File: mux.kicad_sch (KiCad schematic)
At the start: 22 parts, among them U24002 4066, U24003 4066, U24004 4075

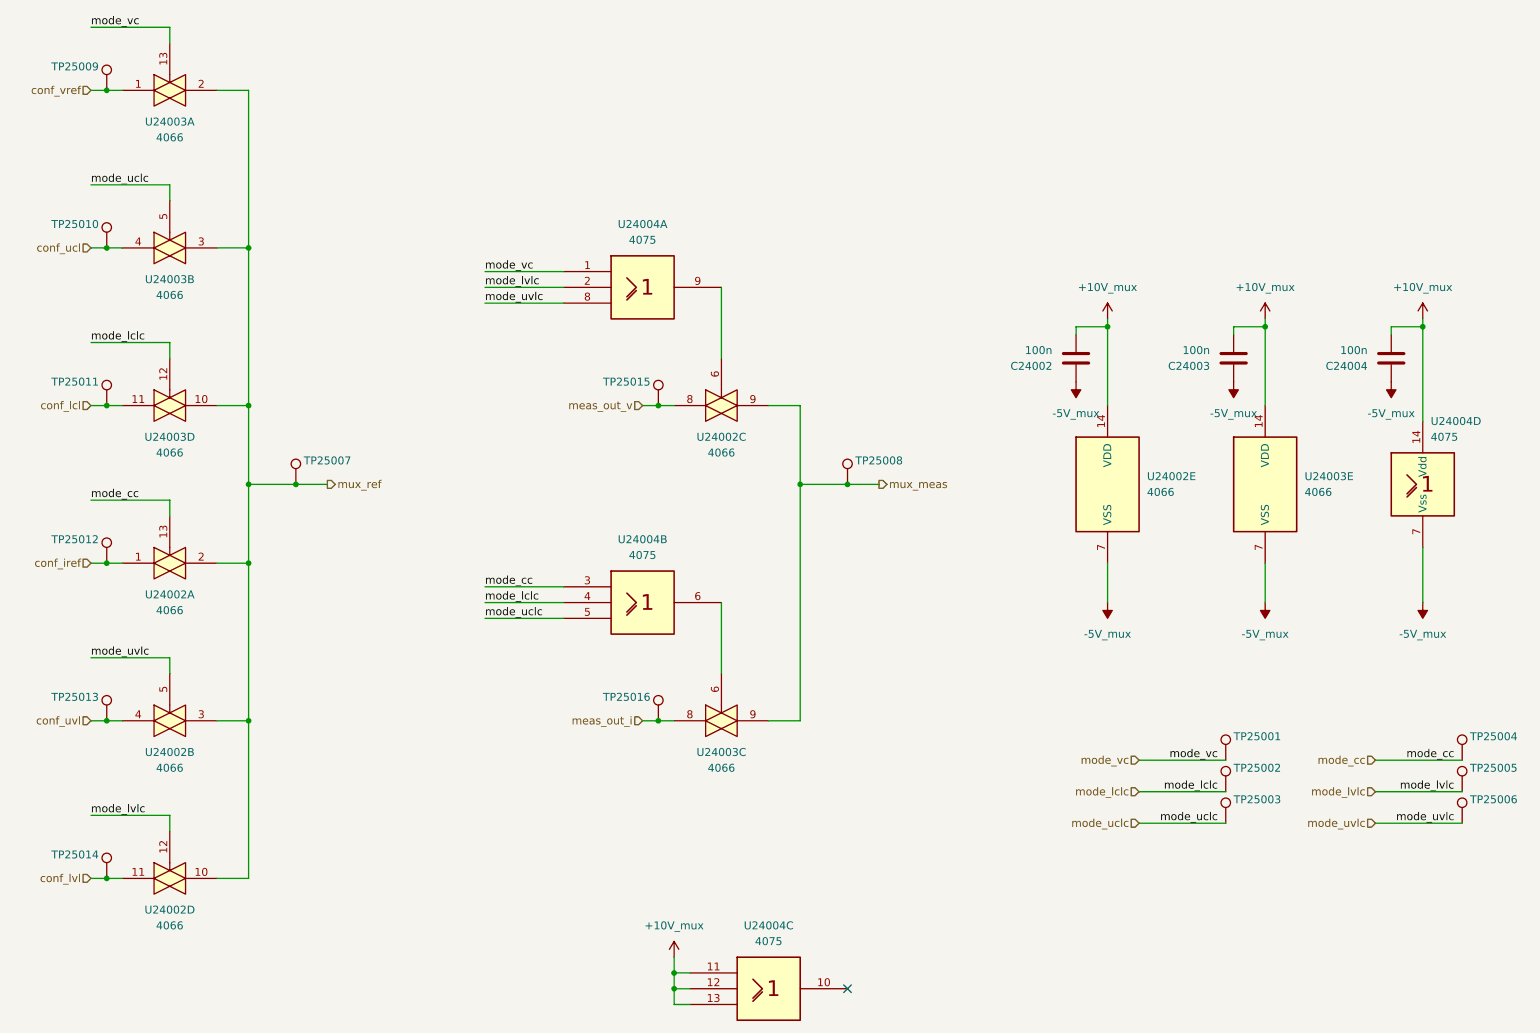
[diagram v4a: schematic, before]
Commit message: edit pss footprint library: export all footprints to library 'pss' and update footprint links
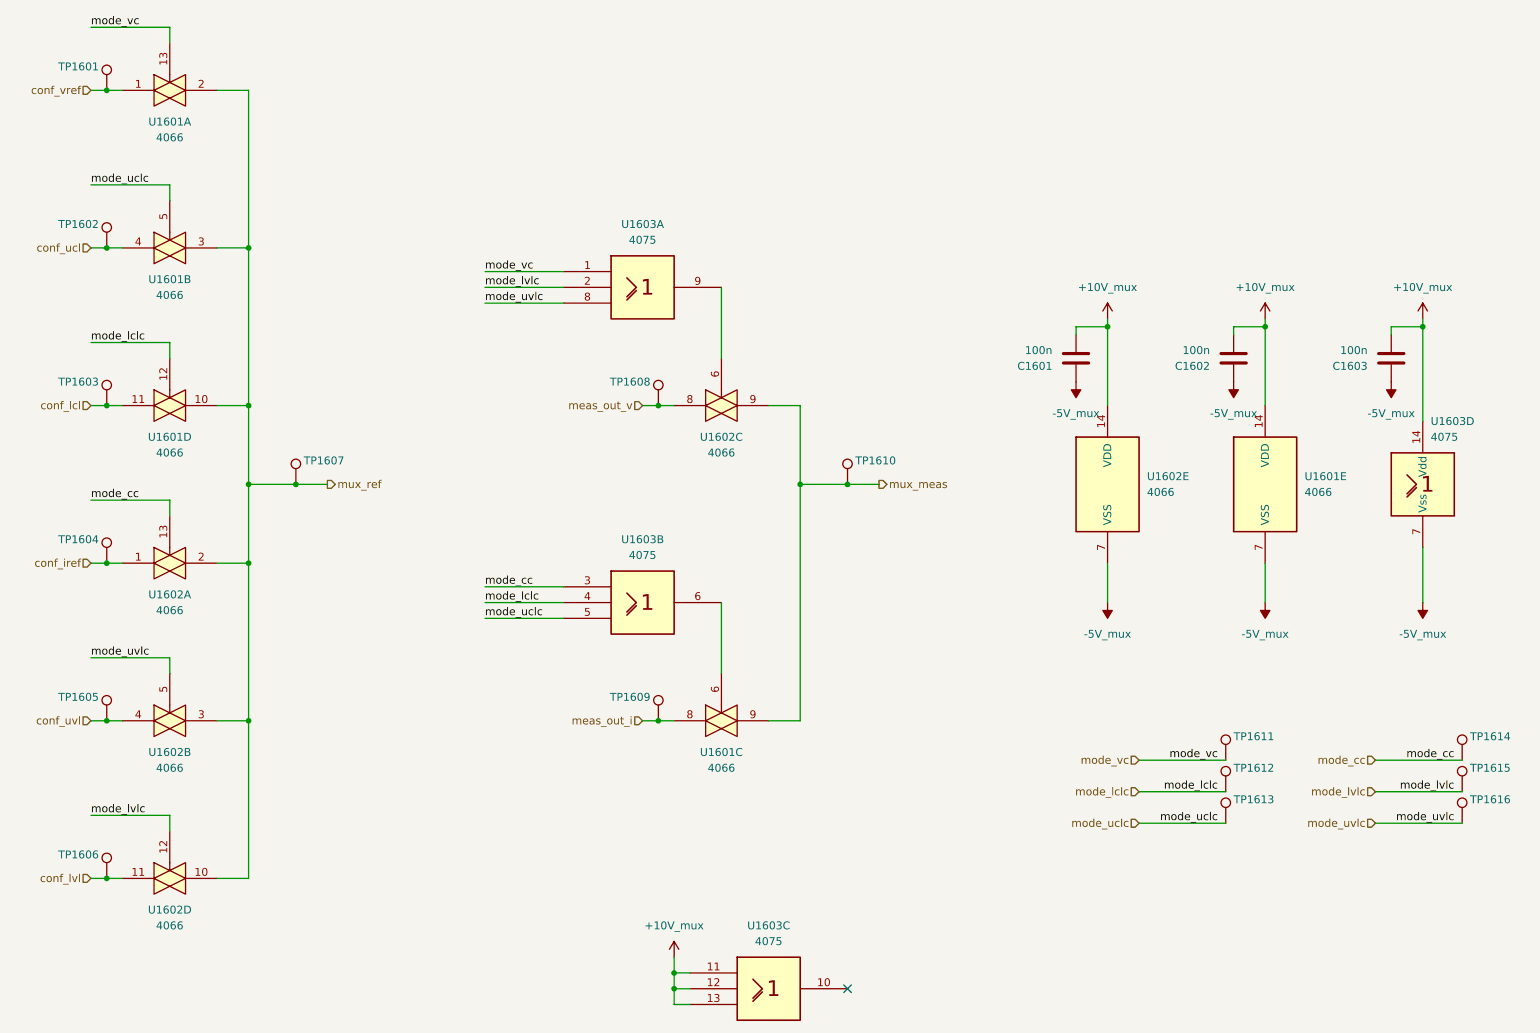
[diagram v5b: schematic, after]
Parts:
- C1601: renamed from C24002; footprint Capacitor_SMD:C_0805_2012Metric_Pad1.18x1.45mm_HandSolder -> pss:C_0805_2012Metric_Pad1.18x1.45mm_HandSolder
- C1602: renamed from C24003; footprint Capacitor_SMD:C_0805_2012Metric_Pad1.18x1.45mm_HandSolder -> pss:C_0805_2012Metric_Pad1.18x1.45mm_HandSolder
- C1603: renamed from C24004; footprint Capacitor_SMD:C_0805_2012Metric_Pad1.18x1.45mm_HandSolder -> pss:C_0805_2012Metric_Pad1.18x1.45mm_HandSolder
- U1601: renamed from U24003; footprint Package_SO:SOIC-14_3.9x8.7mm_P1.27mm -> pss:SOIC-14_3.9x8.7mm_P1.27mm
- U1602: renamed from U24002; footprint Package_SO:SOIC-14_3.9x8.7mm_P1.27mm -> pss:SOIC-14_3.9x8.7mm_P1.27mm
- U1603: renamed from U24004; footprint Package_SO:SOIC-14_3.9x8.7mm_P1.27mm -> pss:SOIC-14_3.9x8.7mm_P1.27mm
- renumbered TP25009 to TP1601, TP25010 to TP1602, TP25011 to TP1603, TP25012 to TP1604, TP25013 to TP1605, TP25014 to TP1606, TP25007 to TP1607, TP25015 to TP1608, TP25016 to TP1609, TP25008 to TP1610, TP25001 to TP1611, TP25002 to TP1612, TP25003 to TP1613, TP25004 to TP1614, TP25005 to TP1615, TP25006 to TP1616
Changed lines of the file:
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@@
 		(dnp no)
 		(fields_autoplaced yes)
-		(property "Reference" "#PWR025007"
+		(property "Reference" "#PWR01601"
 			(at 144.78 187.96 0)
 			(effects
@@
 		(on_board yes)
 		(dnp no)
-		(property "Reference" "TP25006"
+		(property "Reference" "TP1616"
 			(at 273.05 158.75 0)
 			(effects
@@
 		(on_board yes)
 		(dnp no)
-		(property "Reference" "TP25015"
+		(property "Reference" "TP1608"
 			(at 140.97 91.44 0)
 			(effects
@@
 		(dnp no)
 		(fields_autoplaced yes)
-		(property "Reference" "U24002"
+		(property "Reference" "U1602"
 			(at 63.5 151.13 0)
 			(effects
@@
 			)
 		)
-		(property "Footprint" "Package_SO:SOIC-14_3.9x8.7mm_P1.27mm"
+		(property "Footprint" "pss:SOIC-14_3.9x8.7mm_P1.27mm"
 			(at 63.5 146.05 0)
 			(effects
@@
 		(on_board yes)
 		(dnp no)
-		(property "Reference" "TP25016"
+		(property "Reference" "TP1609"
 			(at 140.97 142.24 0)
 			(effects
@@
 		(dnp no)
 		(fields_autoplaced yes)
-		(property "Reference" "U24004"
+		(property "Reference" "U1603"
 			(at 160.02 179.07 0)
 			(effects
@@
 			)
 		)
-		(property "Footprint" "Package_SO:SOIC-14_3.9x8.7mm_P1.27mm"
+		(property "Footprint" "pss:SOIC-14_3.9x8.7mm_P1.27mm"
 			(at 160.02 189.23 0)
 			(effects
@@
 		(dnp no)
 		(fields_autoplaced yes)
-		(property "Reference" "#PWR025015"
+		(property "Reference" "#PWR01610"
 			(at 265.43 123.19 0)
 			(effects
@@
 		(dnp no)
 		(fields_autoplaced yes)
-		(property "Reference" "U24003"
+		(property "Reference" "U1601"
 			(at 63.5 74.93 0)
 			(effects
@@
 			)
 		)
-		(property "Footprint" "Package_SO:SOIC-14_3.9x8.7mm_P1.27mm"
+		(property "Footprint" "pss:SOIC-14_3.9x8.7mm_P1.27mm"
 			(at 63.5 69.85 0)
 			(effects
@@
 		(on_board yes)
 		(dnp no)
-		(property "Reference" "TP25011"
+		(property "Reference" "TP1603"
 			(at 52.07 91.44 0)
 			(effects
@@
 		(dnp no)
 		(fields_autoplaced yes)
-		(property "Reference" "U24004"
+		(property "Reference" "U1603"
 			(at 139.7 116.84 0)
 			(effects
@@
 			)
 		)
-		(property "Footprint" "Package_SO:SOIC-14_3.9x8.7mm_P1.27mm"
+		(property "Footprint" "pss:SOIC-14_3.9x8.7mm_P1.27mm"
 			(at 139.7 127 0)
 			(effects
@@
 		(on_board yes)
 		(dnp no)
-		(property "Reference" "TP25009"
+		(property "Reference" "TP1601"
 			(at 52.07 40.64 0)
 			(effects
@@
 		(dnp no)
 		(fields_autoplaced yes)
-		(property "Reference" "U24004"
+		(property "Reference" "U1603"
 			(at 139.7 66.04 0)
 			(effects
@@
 			)
 		)
-		(property "Footprint" "Package_SO:SOIC-14_3.9x8.7mm_P1.27mm"
+		(property "Footprint" "pss:SOIC-14_3.9x8.7mm_P1.27mm"
 			(at 139.7 76.2 0)
 			(effects
@@
 		(on_board yes)
 		(dnp no)
-		(property "Reference" "TP25002"
+		(property "Reference" "TP1612"
 			(at 234.95 153.67 0)
 			(effects
@@
 		(dnp no)
 		(fields_autoplaced yes)
-		(property "Reference" "#PWR025008"
+		(property "Reference" "#PWR01603"
 			(at 214.63 85.09 0)
 			(effects
@@
 		(dnp no)
 		(fields_autoplaced yes)
-		(property "Reference" "U24002"
+		(property "Reference" "U1602"
 			(at 220.98 106.6799 0)
 			(effects
@@
 			)
 		)
-		(property "Footprint" "Package_SO:SOIC-14_3.9x8.7mm_P1.27mm"
+		(property "Footprint" "pss:SOIC-14_3.9x8.7mm_P1.27mm"
 			(at 214.63 107.95 0)
 			(effects
@@
 		(on_board yes)
 		(dnp no)
-		(property "Reference" "C24004"
+		(property "Reference" "C1603"
 			(at 256.54 88.9001 0)
 			(effects
@@
 			)
 		)
-		(property "Footprint" "Capacitor_SMD:C_0805_2012Metric_Pad1.18x1.45mm_HandSolder"
+		(property "Footprint" "pss:C_0805_2012Metric_Pad1.18x1.45mm_HandSolder"
 			(at 259.3848 83.82 0)
 			(effects
@@
 		(dnp no)
 		(fields_autoplaced yes)
-		(property "Reference" "U24002"
+		(property "Reference" "U1602"
 			(at 152.4 100.33 0)
 			(effects
@@
 			)
 		)
-		(property "Footprint" "Package_SO:SOIC-14_3.9x8.7mm_P1.27mm"
+		(property "Footprint" "pss:SOIC-14_3.9x8.7mm_P1.27mm"
 			(at 152.4 95.25 0)
 			(effects
@@
 		(dnp no)
 		(fields_autoplaced yes)
-		(property "Reference" "#PWR025010"
+		(property "Reference" "#PWR01609"
 			(at 265.43 85.09 0)
 			(effects
@@
 		(dnp no)
 		(fields_autoplaced yes)
-		(property "Reference" "#PWR025002"
+		(property "Reference" "#PWR01605"
 			(at 234.95 87.63 0)
 			(effects
@@
 		(on_board yes)
 		(dnp no)
-		(property "Reference" "TP25003"
+		(property "Reference" "TP1613"
 			(at 234.95 158.75 0)
 			(effects
@@
 		(on_board yes)
 		(dnp no)
-		(property "Reference" "U24004"
+		(property "Reference" "U1603"
 			(at 266.7 97.79 0)
 			(effects
@@
 			)
 		)
-		(property "Footprint" "Package_SO:SOIC-14_3.9x8.7mm_P1.27mm"
+		(property "Footprint" "pss:SOIC-14_3.9x8.7mm_P1.27mm"
 			(at 265.43 107.95 0)
 			(effects
@@
 		(on_board yes)
 		(dnp no)
-		(property "Reference" "TP25010"
+		(property "Reference" "TP1602"
 			(at 52.07 66.04 0)
 			(effects
@@
 		(dnp no)
 		(fields_autoplaced yes)
-		(property "Reference" "U24003"
+		(property "Reference" "U1601"
 			(at 152.4 151.13 0)
 			(effects
@@
 			)
 		)
-		(property "Footprint" "Package_SO:SOIC-14_3.9x8.7mm_P1.27mm"
+		(property "Footprint" "pss:SOIC-14_3.9x8.7mm_P1.27mm"
 			(at 152.4 146.05 0)
 			(effects
@@
 		(dnp no)
 		(fields_autoplaced yes)
-		(property "Reference" "U24002"
+		(property "Reference" "U1602"
 			(at 63.5 176.53 0)
 			(effects
@@
 			)
 		)
-		(property "Footprint" "Package_SO:SOIC-14_3.9x8.7mm_P1.27mm"
+		(property "Footprint" "pss:SOIC-14_3.9x8.7mm_P1.27mm"
 			(at 63.5 171.45 0)
 			(effects
@@
 		(dnp no)
 		(fields_autoplaced yes)
-		(property "Reference" "U24003"
+		(property "Reference" "U1601"
 			(at 246.38 106.6799 0)
 			(effects
@@
 			)
 		)
-		(property "Footprint" "Package_SO:SOIC-14_3.9x8.7mm_P1.27mm"
+		(property "Footprint" "pss:SOIC-14_3.9x8.7mm_P1.27mm"
 			(at 240.03 107.95 0)
 			(effects
@@
 		(on_board yes)
 		(dnp no)
-		(property "Reference" "TP25005"
+		(property "Reference" "TP1615"
 			(at 273.05 153.67 0)
 			(effects
@@
 		(on_board yes)
 		(dnp no)
-		(property "Reference" "TP25013"
+		(property "Reference" "TP1605"
 			(at 52.07 142.24 0)
 			(effects
@@
 		(dnp no)
 		(fields_autoplaced yes)
-		(property "Reference" "#PWR025001"
+		(property "Reference" "#PWR01602"
 			(at 209.55 87.63 0)
 			(effects
@@
 		(on_board yes)
 		(dnp no)
-		(property "Reference" "TP25001"
+		(property "Reference" "TP1611"
 			(at 234.95 148.59 0)
 			(effects
@@
 		(dnp no)
 		(fields_autoplaced yes)
-		(property "Reference" "U24003"
+		(property "Reference" "U1601"
 			(at 63.5 49.53 0)
 			(effects
@@
 			)
 		)
-		(property "Footprint" "Package_SO:SOIC-14_3.9x8.7mm_P1.27mm"
+		(property "Footprint" "pss:SOIC-14_3.9x8.7mm_P1.27mm"
 			(at 63.5 44.45 0)
 			(effects
@@
 		(dnp no)
 		(fields_autoplaced yes)
-		(property "Reference" "#PWR025009"
+		(property "Reference" "#PWR01606"
 			(at 240.03 85.09 0)
 			(effects
@@
 		(dnp no)
 		(fields_autoplaced yes)
-		(property "Reference" "#PWR025003"
+		(property "Reference" "#PWR01608"
 			(at 260.35 87.63 0)
 			(effects
@@
 		(on_board yes)
 		(dnp no)
-		(property "Reference" "C24002"
+		(property "Reference" "C1601"
 			(at 205.74 88.9001 0)
 			(effects
@@
 			)
 		)
-		(property "Footprint" "Capacitor_SMD:C_0805_2012Metric_Pad1.18x1.45mm_HandSolder"
+		(property "Footprint" "pss:C_0805_2012Metric_Pad1.18x1.45mm_HandSolder"
 			(at 208.5848 83.82 0)
 			(effects
@@
 		(on_board yes)
 		(dnp no)
-		(property "Reference" "TP25008"
+		(property "Reference" "TP1610"
 			(at 173.99 104.14 0)
 			(effects
@@
 		(dnp no)
 		(fields_autoplaced yes)
-		(property "Reference" "#PWR025014"
+		(property "Reference" "#PWR01607"
 			(at 240.03 123.19 0)
 			(effects
@@
 		(on_board yes)
 		(dnp no)
-		(property "Reference" "TP25012"
+		(property "Reference" "TP1604"
 			(at 52.07 116.84 0)
 			(effects
@@
 		(on_board yes)
 		(dnp no)
-		(property "Reference" "TP25007"
+		(property "Reference" "TP1607"
 			(at 85.09 104.14 0)
 			(effects
@@
 		(on_board yes)
 		(dnp no)
-		(property "Reference" "C24003"
+		(property "Reference" "C1602"
 			(at 231.14 88.9001 0)
 			(effects
@@
 			)
 		)
-		(property "Footprint" "Capacitor_SMD:C_0805_2012Metric_Pad1.18x1.45mm_HandSolder"
+		(property "Footprint" "pss:C_0805_2012Metric_Pad1.18x1.45mm_HandSolder"
 			(at 233.9848 83.82 0)
 			(effects
@@
 		(dnp no)
 		(fields_autoplaced yes)
-		(property "Reference" "U24003"
+		(property "Reference" "U1601"
 			(at 63.5 100.33 0)
 			(effects
@@
 			)
 		)
-		(property "Footprint" "Package_SO:SOIC-14_3.9x8.7mm_P1.27mm"
+		(property "Footprint" "pss:SOIC-14_3.9x8.7mm_P1.27mm"
 			(at 63.5 95.25 0)
 			(effects
@@
 		(dnp no)
 		(fields_autoplaced yes)
-		(property "Reference" "#PWR025013"
+		(property "Reference" "#PWR01604"
 			(at 214.63 123.19 0)
 			(effects
@@
 		(on_board yes)
 		(dnp no)
-		(property "Reference" "TP25014"
+		(property "Reference" "TP1606"
 			(at 52.07 167.64 0)
 			(effects
@@
 		(on_board yes)
 		(dnp no)
-		(property "Reference" "TP25004"
+		(property "Reference" "TP1614"
 			(at 273.05 148.59 0)
 			(effects
@@
 		(dnp no)
 		(fields_autoplaced yes)
-		(property "Reference" "U24002"
+		(property "Reference" "U1602"
 			(at 63.5 125.73 0)
 			(effects
@@
 			)
 		)
-		(property "Footprint" "Package_SO:SOIC-14_3.9x8.7mm_P1.27mm"
+		(property "Footprint" "pss:SOIC-14_3.9x8.7mm_P1.27mm"
 			(at 63.5 120.65 0)
 			(effects
